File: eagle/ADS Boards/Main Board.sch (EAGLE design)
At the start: 10 parts

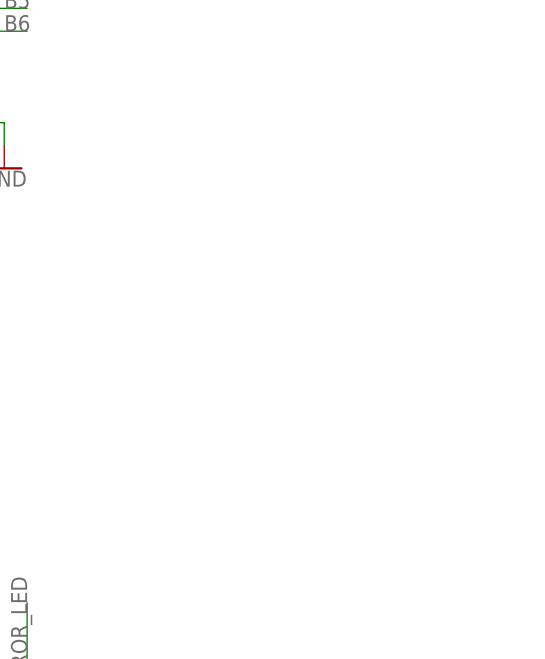
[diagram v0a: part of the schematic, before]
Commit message: Finish Preliminary Board Layouts
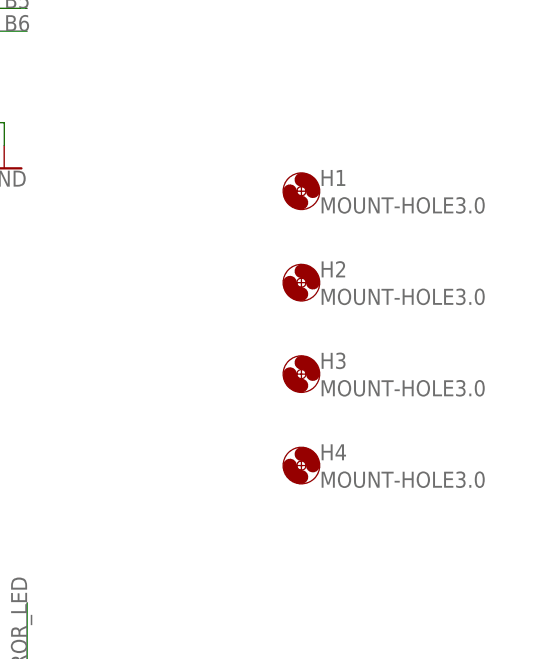
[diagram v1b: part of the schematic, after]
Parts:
- added H1, H2, H3, H4: MOUNT-HOLE3.0, holes:MOUNT-HOLE3.0
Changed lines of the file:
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@@
 <part name="SUPPLY8" library="SparkFun-PowerSymbols" library_urn="urn:adsk.eagle:library:530" deviceset="3.3V" device=""/>
 <part name="GND9" library="SparkFun-PowerSymbols" library_urn="urn:adsk.eagle:library:530" deviceset="GND" device=""/>
+<part name="H1" library="holes" library_urn="urn:adsk.eagle:library:237" deviceset="MOUNT-HOLE" device="3.0" package3d_urn="urn:adsk.eagle:package:14277/1"/>
+<part name="H2" library="holes" library_urn="urn:adsk.eagle:library:237" deviceset="MOUNT-HOLE" device="3.0" package3d_urn="urn:adsk.eagle:package:14277/1"/>
+<part name="H3" library="holes" library_urn="urn:adsk.eagle:library:237" deviceset="MOUNT-HOLE" device="3.0" package3d_urn="urn:adsk.eagle:package:14277/1"/>
+<part name="H4" library="holes" library_urn="urn:adsk.eagle:library:237" deviceset="MOUNT-HOLE" device="3.0" package3d_urn="urn:adsk.eagle:package:14277/1"/>
 </parts>
 <sheets>
@@
 <attribute name="VALUE" x="5.08" y="83.566" size="1.778" layer="96" align="top-center"/>
 </instance>
+<instance part="H1" gate="G$1" x="243.84" y="129.54" smashed="yes">
+<attribute name="NAME" x="245.872" y="130.1242" size="1.778" layer="95"/>
+<attribute name="VALUE" x="245.872" y="127.0762" size="1.778" layer="96"/>
+</instance>
+<instance part="H2" gate="G$1" x="243.84" y="119.38" smashed="yes">
+<attribute name="NAME" x="245.872" y="119.9642" size="1.778" layer="95"/>
+<attribute name="VALUE" x="245.872" y="116.9162" size="1.778" layer="96"/>
+</instance>
+<instance part="H3" gate="G$1" x="243.84" y="109.22" smashed="yes">
+<attribute name="NAME" x="245.872" y="109.8042" size="1.778" layer="95"/>
+<attribute name="VALUE" x="245.872" y="106.7562" size="1.778" layer="96"/>
+</instance>
+<instance part="H4" gate="G$1" x="243.84" y="99.06" smashed="yes">
+<attribute name="NAME" x="245.872" y="99.6442" size="1.778" layer="95"/>
+<attribute name="VALUE" x="245.872" y="96.5962" size="1.778" layer="96"/>
+</instance>
 </instances>

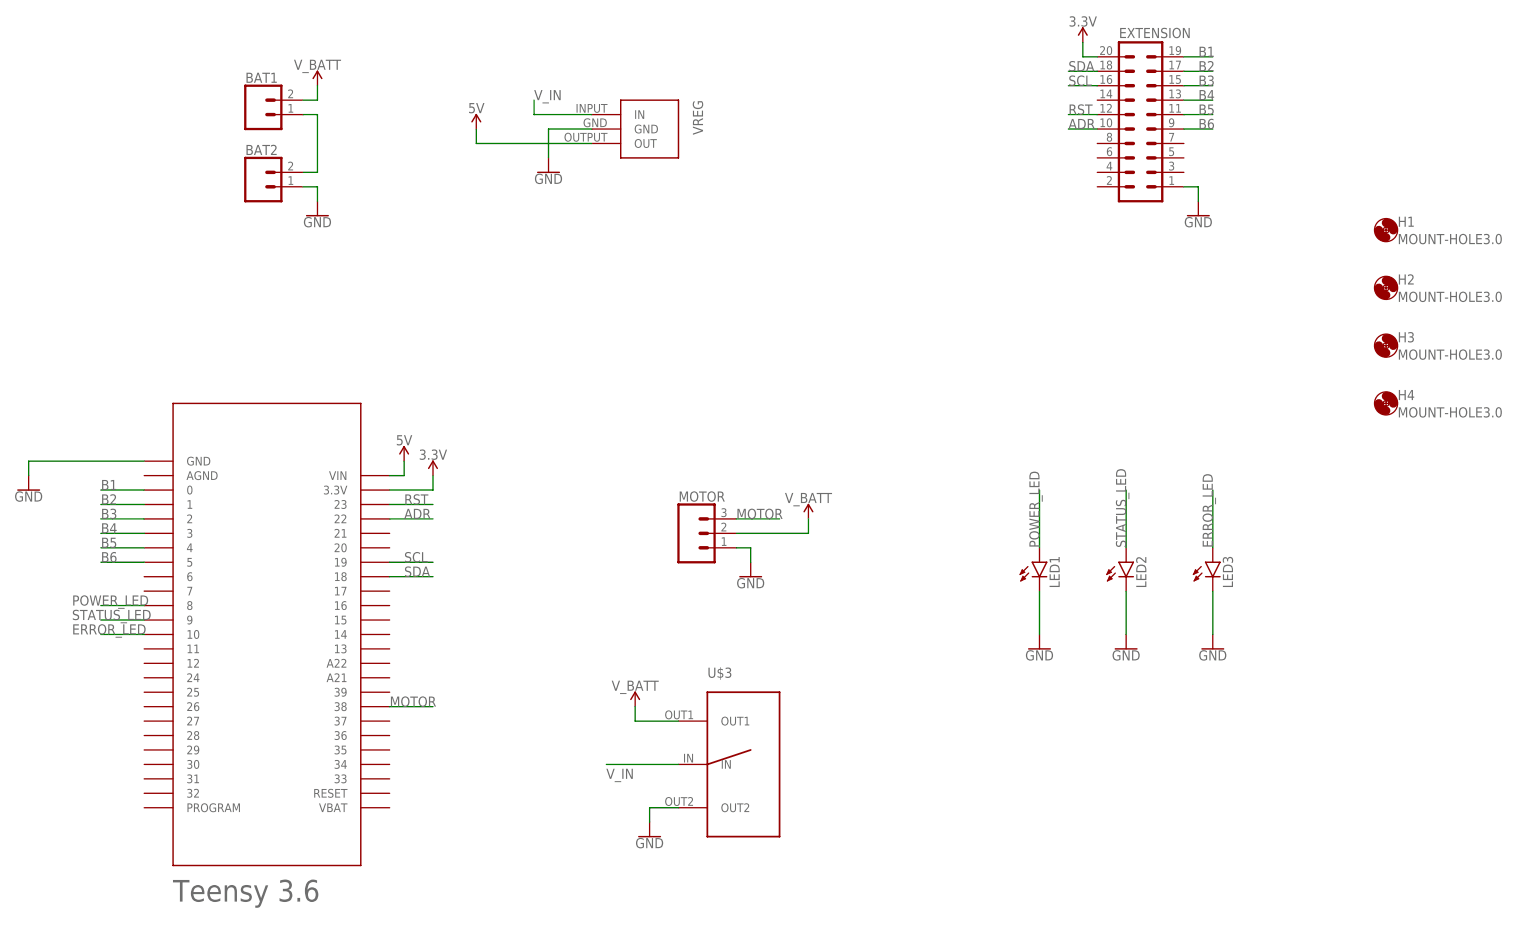
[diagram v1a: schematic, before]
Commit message: Modify to surface mount components
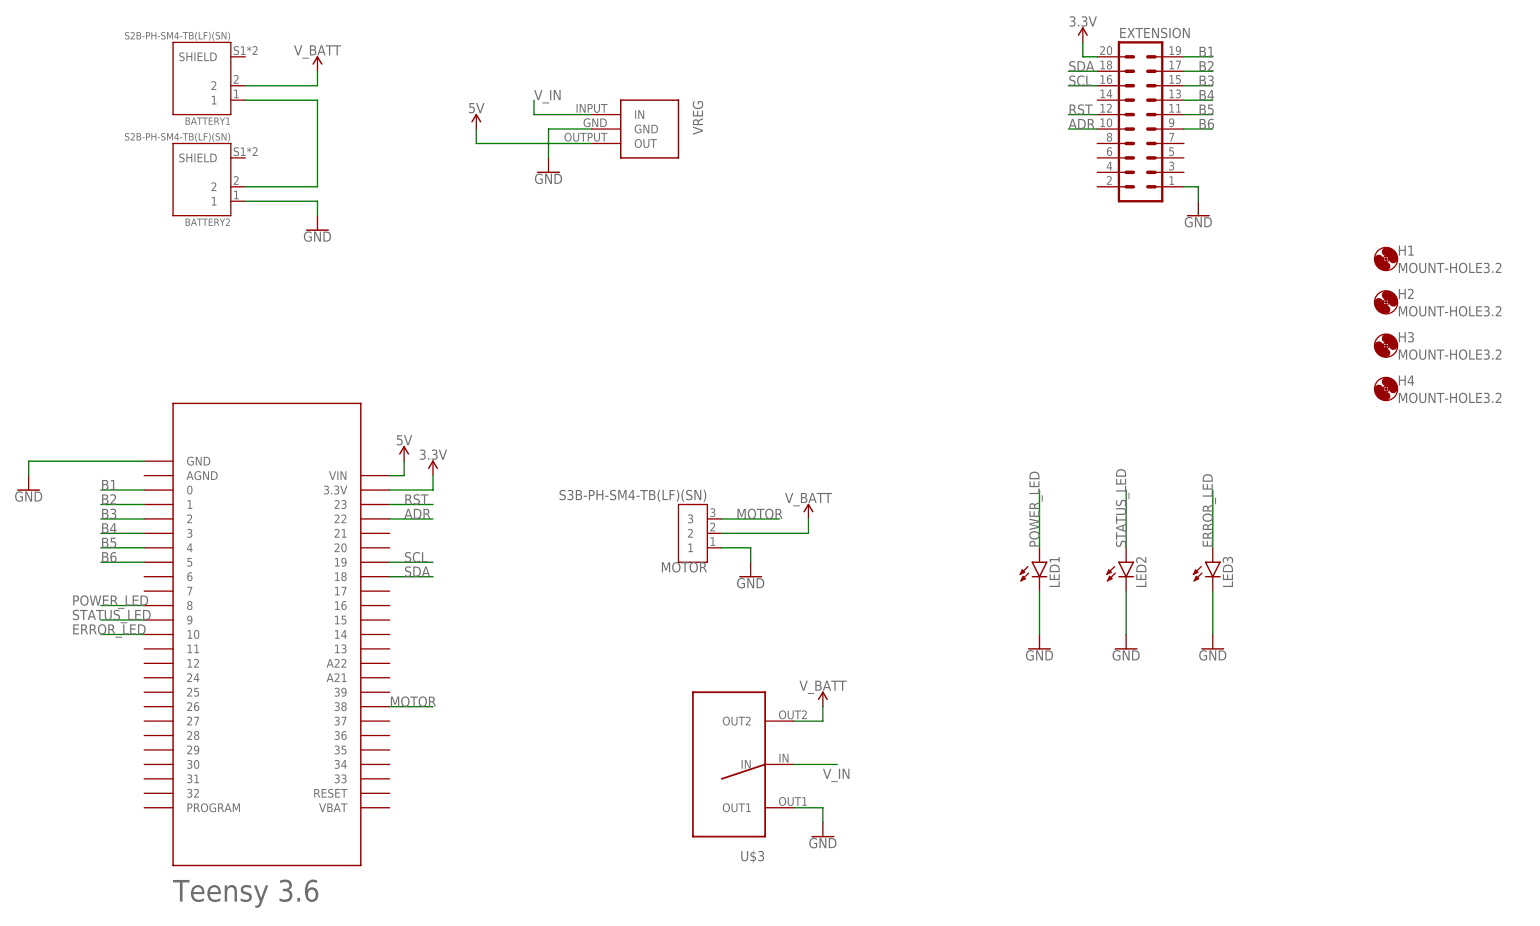
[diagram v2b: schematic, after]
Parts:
- removed BAT1, BAT2: (no value), SparkFun-Connectors:CONN_02JST-PTH-2
- added BATTERY1, BATTERY2: S2B-PH-SM4-TB(LF)(SN), S2B-PH-SM4-TB_LF__SN_:S2B-PH-SM4-TB(LF)(SN)
- H1, H2, H3, H4: value MOUNT-HOLE3.0 -> MOUNT-HOLE3.2; device holes:MOUNT-HOLE3.0 -> holes:MOUNT-HOLE3.2
- MOTOR: value (none) -> S3B-PH-SM4-TB(LF)(SN); device SparkFun-Connectors:CONN_03JST-PTH -> S3B-PH-SM4-TB_LF__SN_:S3B-PH-SM4-TB(LF)(SN)
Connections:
- net GND: now also BATTERY2.1, U$3.OUT1; no longer BAT2.1, U$3.OUT2
- net N$2: now also BATTERY1.1, BATTERY2.2; no longer BAT1.1, BAT2.2
- net V_BATT: now also BATTERY1.2, U$3.OUT2; no longer BAT1.2, U$3.OUT1
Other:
- moved on the sheet: H1, H2, H4, U$3

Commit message: Add files via upload
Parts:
- added C1: 0.33µF, SparkFun-Capacitors:0.33UF/330NF-0805-50V-10%
- added C2: 0.1uF, SparkFun-Capacitors:0.1UF-0603-25V-5%
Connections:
- net 5V: now also C2.1
- net GND: now also C1.2, C2.2
- net V_IN: now also C1.1
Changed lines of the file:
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@@
 <?xml version="1.0" encoding="utf-8"?>
 <!DOCTYPE eagle SYSTEM "eagle.dtd">
-<eagle version="9.2.2">
+<eagle version="9.1.3">
 <drawing>
 <settings>
@@
 <part name="BATTERY2" library="S2B-PH-SM4-TB_LF__SN_" deviceset="S2B-PH-SM4-TB(LF)(SN)" device=""/>
 <part name="MOTOR" library="S3B-PH-SM4-TB_LF__SN_" deviceset="S3B-PH-SM4-TB(LF)(SN)" device=""/>
+<part name="C1" library="SparkFun-Capacitors" deviceset="0.33UF/330NF" device="-0805-50V-10%" value="0.33µF"/>
+<part name="C2" library="SparkFun-Capacitors" deviceset="0.1UF" device="-0603-25V-5%" value="0.1uF"/>
+<part name="GND10" library="SparkFun-PowerSymbols" deviceset="GND" device=""/>
+<part name="GND11" library="SparkFun-PowerSymbols" deviceset="GND" device=""/>
 </parts>
 <sheets>
@@
 <attribute name="VALUE" x="219.075" y="66.548" size="1.778" layer="96" rot="R90"/>
 </instance>
-<instance part="U$2" gate="G$1" x="119.38" y="152.4" smashed="yes" rot="R180"/>
+<instance part="U$2" gate="G$1" x="106.68" y="154.94" smashed="yes" rot="R270"/>
 <instance part="U$3" gate="G$1" x="129.54" y="35.56" smashed="yes" rot="R90">
 <attribute name="NAME" x="134.62" y="20.32" size="1.778" layer="95" rot="R180"/>
@@
 <attribute name="VALUE" x="55.88" y="129.286" size="1.778" layer="96" align="top-center"/>
 </instance>
-<instance part="GND3" gate="1" x="96.52" y="139.7" smashed="yes">
-<attribute name="VALUE" x="96.52" y="139.446" size="1.778" layer="96" align="top-center"/>
+<instance part="GND3" gate="1" x="111.76" y="127" smashed="yes">
+<attribute name="VALUE" x="111.76" y="126.746" size="1.778" layer="96" align="top-center"/>
 </instance>
 <instance part="GND4" gate="1" x="132.08" y="68.58" smashed="yes">
@@
 <attribute name="VALUE" x="71.12" y="91.694" size="1.778" layer="96" align="bottom-center"/>
 </instance>
-<instance part="SUPPLY7" gate="G$1" x="83.82" y="147.32" smashed="yes" rot="MR0">
-<attribute name="VALUE" x="83.82" y="150.114" size="1.778" layer="96" rot="MR0" align="bottom-center"/>
+<instance part="SUPPLY7" gate="G$1" x="127" y="142.24" smashed="yes" rot="MR0">
+<attribute name="VALUE" x="127" y="145.034" size="1.778" layer="96" rot="MR0" align="bottom-center"/>
 </instance>
 <instance part="SUPPLY8" gate="G$1" x="76.2" y="86.36" smashed="yes">
@@
 <attribute name="VALUE" x="124.46335" y="83.830040625" size="1.780340625" layer="96" rot="R180"/>
 </instance>
+<instance part="C1" gate="G$1" x="93.98" y="134.62"/>
+<instance part="C2" gate="G$1" x="127" y="134.62"/>
+<instance part="GND10" gate="1" x="93.98" y="127"/>
+<instance part="GND11" gate="1" x="127" y="127"/>
 </instances>
 <busses>
@@
 <segment>
 <pinref part="U$2" gate="G$1" pin="GND"/>
-<wire x1="104.14" y1="147.32" x2="96.52" y2="147.32" width="0.1524" layer="91"/>
+<wire x1="111.76" y1="139.7" x2="111.76" y2="134.62" width="0.1524" layer="91"/>
 <pinref part="GND3" gate="1" pin="GND"/>
-<wire x1="96.52" y1="147.32" x2="96.52" y2="142.24" width="0.1524" layer="91"/>
+<wire x1="111.76" y1="134.62" x2="111.76" y2="129.54" width="0.1524" layer="91"/>
 </segment>
 <segment>
@@
 <wire x1="182.88" y1="66.04" x2="182.88" y2="58.42" width="0.1524" layer="91"/>
 </segment>
+<segment>
+<pinref part="C1" gate="G$1" pin="2"/>
+<pinref part="GND10" gate="1" pin="GND"/>
+<wire x1="93.98" y1="132.08" x2="93.98" y2="129.54" width="0.1524" layer="91"/>
+</segment>
+<segment>
+<pinref part="C2" gate="G$1" pin="2"/>
+<pinref part="GND11" gate="1" pin="GND"/>
+<wire x1="127" y1="132.08" x2="127" y2="129.54" width="0.1524" layer="91"/>
+</segment>
 </net>
 <net name="3.3V" class="0">
@@
 <pinref part="U$2" gate="G$1" pin="OUT"/>
 <pinref part="SUPPLY7" gate="G$1" pin="5V"/>
-<wire x1="104.14" y1="144.78" x2="83.82" y2="144.78" width="0.1524" layer="91"/>
-<wire x1="83.82" y1="144.78" x2="83.82" y2="147.32" width="0.1524" layer="91"/>
+<wire x1="114.3" y1="139.7" x2="127" y2="139.7" width="0.1524" layer="91"/>
+<wire x1="127" y1="139.7" x2="127" y2="142.24" width="0.1524" layer="91"/>
+<junction x="127" y="139.7"/>
+<pinref part="C2" gate="G$1" pin="1"/>
 </segment>
 </net>
@@
 </segment>
 <segment>
+<label x="93.98" y="142.24" size="1.778" layer="95"/>
+<wire x1="93.98" y1="139.7" x2="93.98" y2="142.24" width="0.1524" layer="91"/>
+<pinref part="C1" gate="G$1" pin="1"/>
+<junction x="93.98" y="139.7"/>
 <pinref part="U$2" gate="G$1" pin="IN"/>
-<wire x1="104.14" y1="149.86" x2="93.98" y2="149.86" width="0.1524" layer="91"/>
-<label x="93.98" y="152.4" size="1.778" layer="95"/>
-<wire x1="93.98" y1="149.86" x2="93.98" y2="152.4" width="0.1524" layer="91"/>
-</segment>
-</net>
+<wire x1="109.22" y1="139.7" x2="93.98" y2="139.7" width="0.1524" layer="91"/>
+</segment>
+</net>
